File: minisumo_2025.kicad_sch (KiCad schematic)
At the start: 95 parts, among them J1 USB_C Connector, J10 DISTANCE_R90, J11 DISTANCE_R, J12 DISTANCE_RF, J13 DISTANCE_L90, J14 DISTANCE_L, J15 LINE_LEFT, J16 DISTANCE_LF, J2 SERVO, J3 START_MODULE, J4 MOTOR1, J5 MOTOR2, J6 BATT_IN, J8 DISTANCE_CENTER, J9 LINE_RIGHT, SW1 RESET, SW2 CASE, SW5 BOOT, U1 LMR33630ADDAR, U2 USBLC6-2P6, U3 ESP32-S3-WROOM-1, U4 TLV75730PDBVR, U5 TXS0108ERGYR, U6 DRIVER 1, U7 DRIVER 2

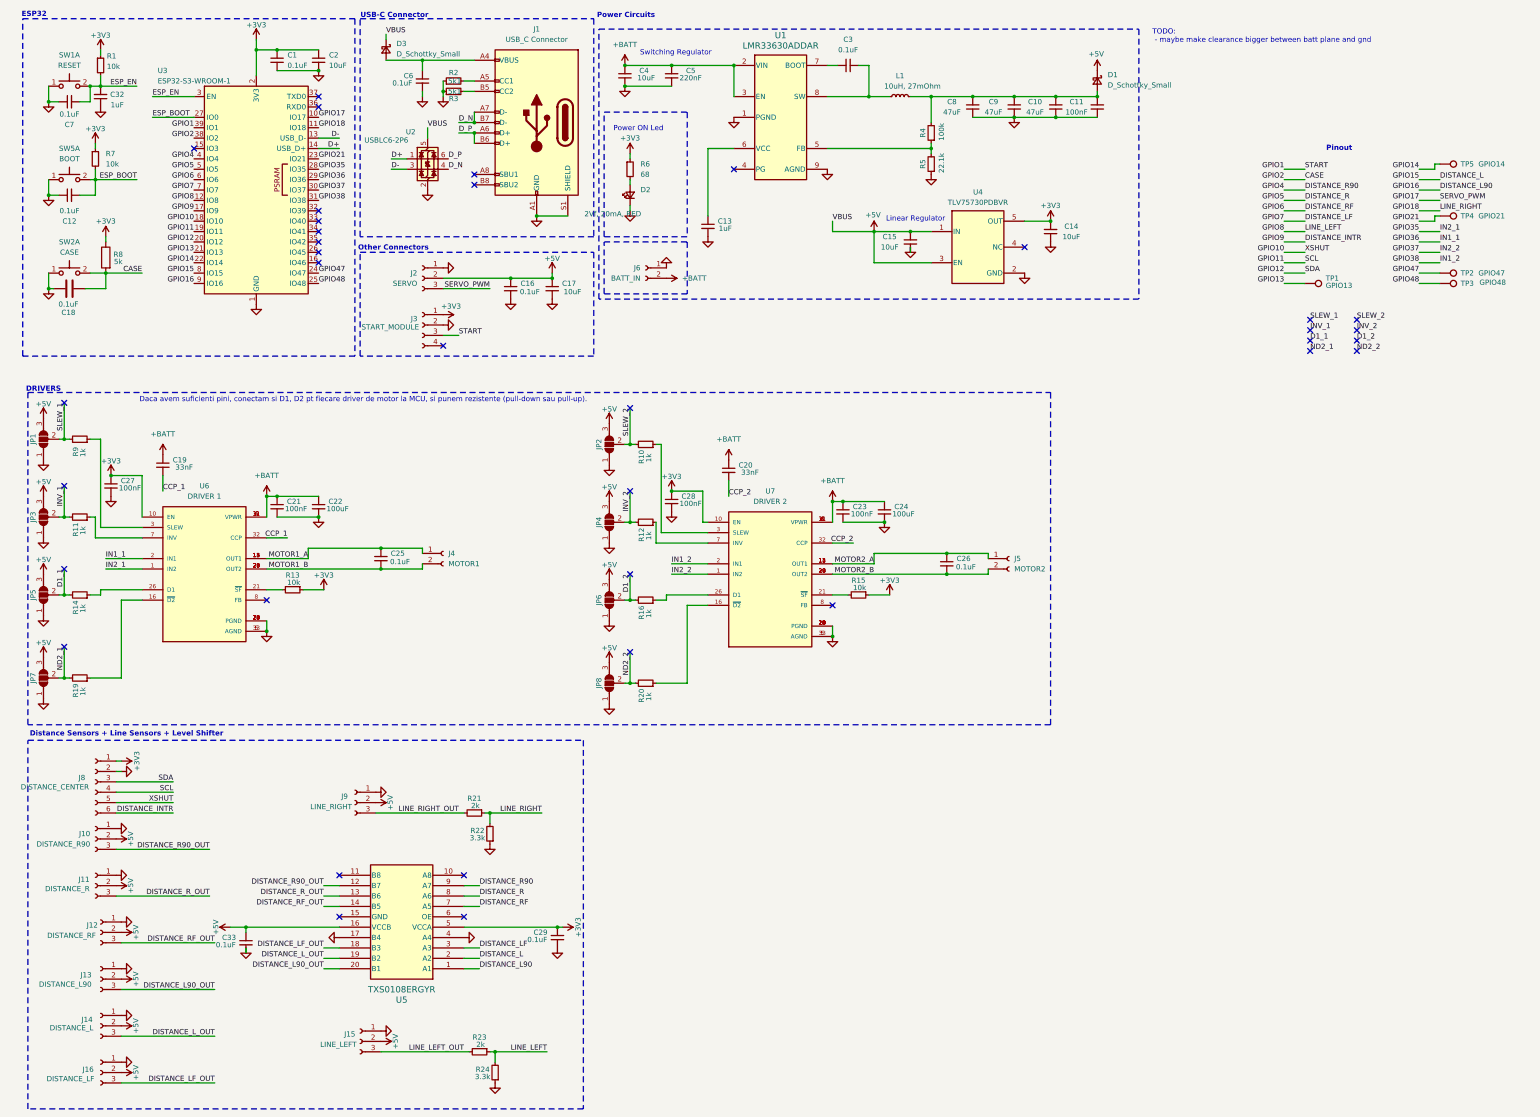
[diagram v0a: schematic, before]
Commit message: added leds for power
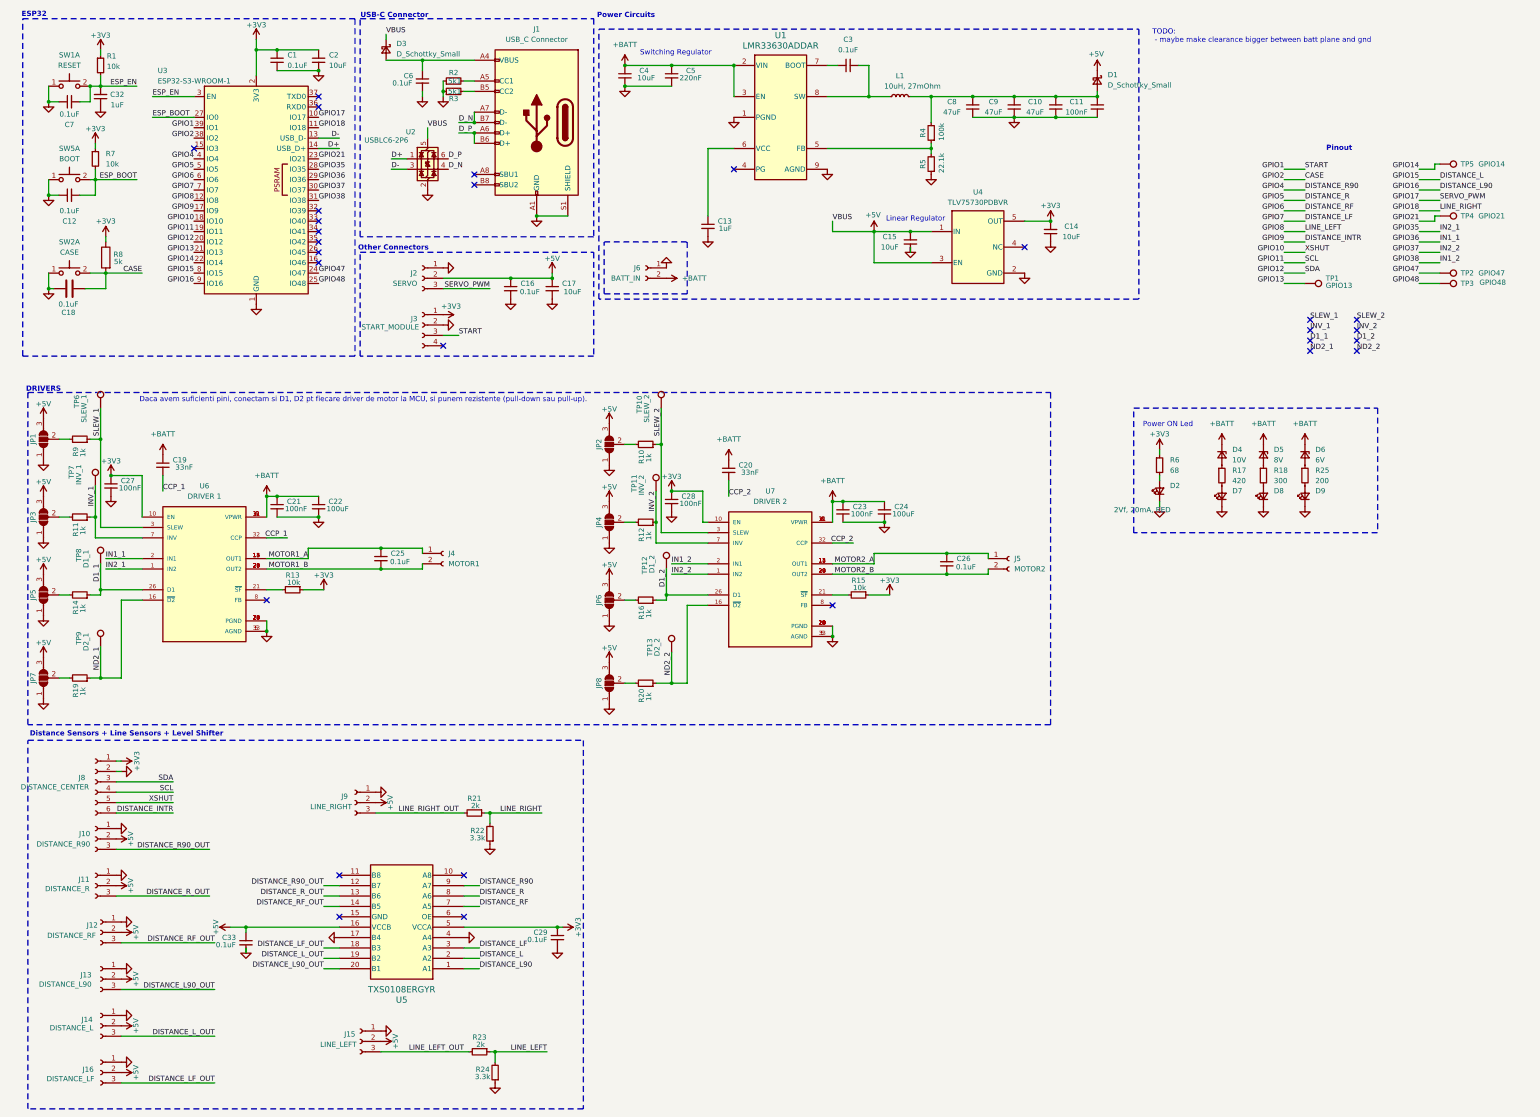
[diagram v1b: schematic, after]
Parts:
- added D4: 10V, Diode_SMD:D_0402_1005Metric, symbol Device:D_Zener_Small
- added D5: 8V, Diode_SMD:D_0402_1005Metric, symbol Device:D_Zener_Small
- added D6: 6V, Diode_SMD:D_0402_1005Metric, symbol Device:D_Zener_Small
- added D7, D8, D9: 2Vf, 20mA, RED, LED_SMD:LED_0603_1608Metric, symbol Device:LED_Small
- added R17: 420, Resistor_SMD:R_0402_1005Metric, symbol Device:R_Small
- added R18: 300, Resistor_SMD:R_0402_1005Metric, symbol Device:R_Small
- added R25: 200, Resistor_SMD:R_0402_1005Metric, symbol Device:R_Small
- added TP10: SLEW_2, TestPoint:TestPoint_Pad_1.5x1.5mm, symbol Connector:TestPoint
- added TP11: INV_2, TestPoint:TestPoint_Pad_1.5x1.5mm, symbol Connector:TestPoint
- added TP12: D1_2, TestPoint:TestPoint_Pad_1.5x1.5mm, symbol Connector:TestPoint
- added TP13: D2_2, TestPoint:TestPoint_Pad_1.5x1.5mm, symbol Connector:TestPoint
- added TP6: SLEW_1, TestPoint:TestPoint_Pad_1.5x1.5mm, symbol Connector:TestPoint
- added TP7: INV_1, TestPoint:TestPoint_Pad_1.5x1.5mm, symbol Connector:TestPoint
- added TP8: D1_1, TestPoint:TestPoint_Pad_1.5x1.5mm, symbol Connector:TestPoint
- added TP9: D2_1, TestPoint:TestPoint_Pad_1.5x1.5mm, symbol Connector:TestPoint
- D2: footprint (none) -> LED_SMD:LED_0603_1608Metric
- R6: footprint (none) -> Resistor_SMD:R_0402_1005Metric
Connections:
- net +BATT: now also D4.1 (K), D5.1 (K), D6.1 (K)
- net D1_1: now also R14.1, U6.26 (D1), TP8.1; no longer JP5.2 (C), R14.2
- net D1_2: now also R16.1, U7.26 (D1), TP12.1; no longer JP6.2 (C), R16.2
- net GND: now also D7.1 (K), D8.1 (K), D9.1 (K)
- net INV_1: now also R11.1, U6.7 (INV), TP7.1; no longer JP3.2 (C), R11.2
- net INV_2: now also R12.1, U7.7 (INV), TP11.1; no longer JP4.2 (C), R12.2
- net ND2_1: now also R19.1, U6.16 (~{D2}), TP9.1; no longer JP7.2 (C), R19.2
- net ND2_2: now also R20.1, U7.16 (~{D2}), TP13.1; no longer JP8.2 (C), R20.2
- net SLEW_1: now also R9.1, U6.3 (SLEW), TP6.1; no longer JP1.2 (C), R9.2
- net SLEW_2: now also R10.1, U7.3 (SLEW), TP10.1; no longer JP2.2 (C), R10.2
- new net: JP7.2 (C), R19.2
- new net: JP2.2 (C), R10.2
- new net: JP3.2 (C), R11.2
- new net: JP4.2 (C), R12.2
- new net: D5.2 (A), R18.1
- new net: D9.2 (A), R25.2
- new net: JP8.2 (C), R20.2
- new net: JP1.2 (C), R9.2
- new net: D8.2 (A), R18.2
- new net: JP5.2 (C), R14.2
- new net: JP6.2 (C), R16.2
- new net: D6.2 (A), R25.1
- new net: D4.2 (A), R17.1
- new net: D7.2 (A), R17.2
- no-connect marks 36 -> 28

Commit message: finished layout
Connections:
- net GND: now also U5.15 (GND), U5.6 (OE); no longer U5.17 (B4), U5.4 (A4)
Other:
- note added: "TODO:"
- note removed: "TODO: - maybe make clearance bigger between batt plane and gnd"

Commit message: silkscreen
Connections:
- net +3V3: now also U5.6 (OE)
- net GND: no longer U5.6 (OE)

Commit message: backup
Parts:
- C1, C12, C16, C18, C25, C26, C29, C3, C33, C6, C7: LCSC Part Number (none) -> C1525
- C10, C8, C9: LCSC Part Number (none) -> C77101
- C11, C21, C23, C27, C28: LCSC Part Number (none) -> C77050
- C13: LCSC Part Number (none) -> C92759
- C14, C15, C17, C4: LCSC Part Number (none) -> C437568
- C19, C20: LCSC Part Number (none) -> C1614
- C2: footprint Capacitor_SMD:C_0402_1005Metric -> Capacitor_SMD:C_0603_1608Metric; LCSC Part Number (none) -> C70225
- C22, C24, J10, J11, J12, J13, J14, J15, J16, J2, J3, J4, J5, J6, J8, J9, JP1, JP2, JP3, JP4, JP5, JP6, JP7, JP8, TP1, TP10, TP11, TP12, TP13, TP2, TP3, TP4, TP5, TP6, TP7, TP8, TP9: now not fitted
- C32: LCSC Part Number (none) -> C14445
- C5: LCSC Part Number (none) -> C1770
- D1, D3: LCSC Part Number (none) -> C389355
- D2, D7, D8, D9: LCSC Part Number (none) -> C2286
- D4: footprint Diode_SMD:D_0402_1005Metric -> Diode_SMD:Nexperia_CFP3_SOD-123W; LCSC Part Number (none) -> C173431
- D5: value 8V -> 8.2V; footprint Diode_SMD:D_0402_1005Metric -> Diode_SMD:Nexperia_CFP3_SOD-123W; LCSC Part Number (none) -> C19077406
- D6: footprint Diode_SMD:D_0402_1005Metric -> Diode_SMD:Nexperia_CFP3_SOD-123W; LCSC Part Number (none) -> C115277
- J1: LCSC Part Number (none) -> C165948
- L1: LCSC Part Number (none) -> C5329540
- R1, R13, R15, R7: LCSC Part Number (none) -> C25531
- R10, R11, R12, R14, R16, R19, R20, R9: LCSC Part Number (none) -> C11702
- R17: value 420 -> 412; LCSC Part Number (none) -> C25112
- R18: LCSC Part Number (none) -> C25102
- R2, R3: footprint Resistor_SMD:R_0603_1608Metric -> Resistor_SMD:R_0402_1005Metric; LCSC Part Number (none) -> C25905
- R21, R23: LCSC Part Number (none) -> C4109
- R22, R24: LCSC Part Number (none) -> C25890
- R25: LCSC Part Number (none) -> C25087
- R4: LCSC Part Number (none) -> C481918
- R5: LCSC Part Number (none) -> C844504
- R6: LCSC Part Number (none) -> C25131
- R8: LCSC Part Number (none) -> C477765
- SW1, SW2, SW5: LCSC Part Number (none) -> C720477
- U1: LCSC Part Number (none) -> C841384
- U2: LCSC Part Number (none) -> C15999
- U3: LCSC Part Number (none) -> C701341
- U4: LCSC Part Number (none) -> C485517
- U5: LCSC Part Number (none) -> C90706
- U6: value DRIVER 1 -> MC33926PNB; LCSC Part Number (none) -> C1556870
- U7: value DRIVER 2 -> MC33926PNB; LCSC Part Number (none) -> C1556870

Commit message: final.
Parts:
- C1, C12, C16, C18, C25, C26, C29, C3, C33, C6, C7: LCSC Part # (none) -> C1525; LCSC Part Number C1525 -> (none)
- C10, C8, C9: LCSC Part # (none) -> C77101; LCSC Part Number C77101 -> (none)
- C11, C21, C23, C27, C28: LCSC Part # (none) -> C77050; LCSC Part Number C77050 -> (none)
- C13: LCSC Part # (none) -> C92759; LCSC Part Number C92759 -> (none)
- C14, C15, C17, C4: LCSC Part # (none) -> C437568; LCSC Part Number C437568 -> (none)
- C19, C20: LCSC Part # (none) -> C1614; LCSC Part Number C1614 -> (none)
- C2: LCSC Part # (none) -> C70225; LCSC Part Number C70225 -> (none)
- C32: LCSC Part # (none) -> C14445; LCSC Part Number C14445 -> (none)
- C5: LCSC Part # (none) -> C1770; LCSC Part Number C1770 -> (none)
- D1, D3: LCSC Part # (none) -> C389355; LCSC Part Number C389355 -> (none)
- D2, D7, D8, D9: LCSC Part # (none) -> C2286; LCSC Part Number C2286 -> (none)
- D4: LCSC Part # (none) -> C173431; LCSC Part Number C173431 -> (none)
- D5: LCSC Part # (none) -> C19077406; LCSC Part Number C19077406 -> (none)
- D6: LCSC Part # (none) -> C115277; LCSC Part Number C115277 -> (none)
- J1: LCSC Part # (none) -> C165948; LCSC Part Number C165948 -> (none)
- L1: LCSC Part # (none) -> C5329540; LCSC Part Number C5329540 -> (none)
- R1, R13, R15, R7: LCSC Part # (none) -> C25531; LCSC Part Number C25531 -> (none)
- R10, R11, R12, R14, R16, R19, R20, R9: LCSC Part # (none) -> C11702; LCSC Part Number C11702 -> (none)
- R17: LCSC Part # (none) -> C25112; LCSC Part Number C25112 -> (none)
- R18: LCSC Part # (none) -> C25102; LCSC Part Number C25102 -> (none)
- R2, R3: LCSC Part # (none) -> C25905; LCSC Part Number C25905 -> (none)
- R21, R23: LCSC Part # (none) -> C4109; LCSC Part Number C4109 -> (none)
- R22, R24: LCSC Part # (none) -> C25890; LCSC Part Number C25890 -> (none)
- R25: LCSC Part # (none) -> C25087; LCSC Part Number C25087 -> (none)
- R4: LCSC Part # (none) -> C481918; LCSC Part Number C481918 -> (none)
- R5: LCSC Part # (none) -> C844504; LCSC Part Number C844504 -> (none)
- R6: LCSC Part # (none) -> C25131; LCSC Part Number C25131 -> (none)
- R8: LCSC Part # (none) -> C477765; LCSC Part Number C477765 -> (none)
- SW1, SW2, SW5: LCSC Part # (none) -> C720477; LCSC Part Number C720477 -> (none)
- U1: LCSC Part # (none) -> C841384; LCSC Part Number C841384 -> (none)
- U2: LCSC Part # (none) -> C15999; LCSC Part Number C15999 -> (none)
- U3: LCSC Part # (none) -> C701341; LCSC Part Number C701341 -> (none)
- U4: LCSC Part # (none) -> C485517; LCSC Part Number C485517 -> (none)
- U5: LCSC Part # (none) -> C90706; LCSC Part Number C90706 -> (none)
- U6, U7: LCSC Part # (none) -> C1556870; LCSC Part Number C1556870 -> (none)

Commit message: saved required changes
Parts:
- removed C33: 0.1uF, Capacitor_SMD:C_0402_1005Metric, symbol Device:C_Small
- removed U5: TXS0108ERGYR, footprints:DQS20_TEX, symbol 2025-02-16_00-59-53:TXB0108DQSR
- added C30: 0.1uF, Capacitor_SMD:C_0402_1005Metric, symbol Device:C_Small
- added U5: TXS0108EPWR, footprints:SOP65P640X120-20N, symbol TXS0108EPWR:TXS0108EPWR
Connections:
- net GPIO35 is gone; now on net GPIO13: U3.28 (IO35), U6.1 (IN2)
- net GPIO36 is gone; now on net GPIO14: U3.29 (IO36), U6.2 (IN1)
- net +3V3: now also U5.10 (OE), U5.2 (VCCA)
- net +5V: now also C30.1, U5.19 (VCCB)
- net DISTANCE_L: now also U3.5 (IO5), U5.3 (A2); no longer U3.8 (IO15)
- net DISTANCE_L90: now also U3.4 (IO4), U5.1 (A1); no longer U3.9 (IO16)
- net DISTANCE_L90_OUT: now also U5.20 (B1)
- net DISTANCE_LF: now also U3.6 (IO6), U5.4 (A3); no longer U3.7 (IO7)
- net DISTANCE_LF_OUT: now also U5.17 (B3)
- net DISTANCE_L_OUT: now also U5.18 (B2)
- net DISTANCE_R: now also U3.8 (IO15), U5.7 (A6); no longer U3.5 (IO5)
- net DISTANCE_R90: now also U3.9 (IO16), U5.8 (A7); no longer U3.4 (IO4)
- net DISTANCE_R90_OUT: now also U5.13 (B7)
- net DISTANCE_RF: now also U3.7 (IO7), U5.6 (A5); no longer U3.6 (IO6)
- net DISTANCE_RF_OUT: now also U5.15 (B5)
- net DISTANCE_R_OUT: now also U5.14 (B6)
- net GND: now also C30.2, U5.11 (GND); no longer J1.S1 (SHIELD), R22.1
- no-connect marks 28 -> 29
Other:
- moved on the sheet: J15, R23, R24

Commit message: more
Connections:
- net GPIO37 is gone; now on net GPIO21: U3.30 (IO37), U7.1 (IN2)
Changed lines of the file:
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@@
 	(wire
 		(pts
-			(xy 355.6 72.39) (xy 360.68 72.39)
+			(xy 355.6 72.39) (xy 374.65 72.39)
 		)
 		(stroke
@@
 		(effects
 			(font
+				(size 1.27 1.27)
+			)
+			(justify left bottom)
+		)
+	)
+	(label "GPIO21"
+		(at 374.65 72.39 0)
+		(effects
+			(font

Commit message: test board layout
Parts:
- removed C16: 0.1uF, Capacitor_SMD:C_0402_1005Metric, symbol Device:C_Small
- removed C17: 10uF, Capacitor_SMD:C_1210_3225Metric, symbol Device:C_Small
- removed J2: SERVO, Connector_JST:JST_XH_B3B-XH-A_1x03_P2.50mm_Vertical, symbol Connector:Conn_01x03_Socket
- removed JP5, JP6, JP7, JP8: SolderJumper_3_Open, Jumper:SolderJumper-3_P1.3mm_Open_RoundedPad1.0x1.5mm_NumberLabels, symbol Jumper:SolderJumper_3_Open
- removed TP2: GPIO47, TestPoint:TestPoint_Pad_1.5x1.5mm, symbol Connector:TestPoint
- removed TP3: GPIO48, TestPoint:TestPoint_Pad_1.5x1.5mm, symbol Connector:TestPoint
- removed TP4: GPIO21, TestPoint:TestPoint_Pad_1.5x1.5mm, symbol Connector:TestPoint
- removed TP5: GPIO14, TestPoint:TestPoint_Pad_1.5x1.5mm, symbol Connector:TestPoint
- added C31: 4.7uF, Capacitor_SMD:C_1210_3225Metric, symbol Device:C_Small
- added C33: 10uF, Capacitor_THT:C_Radial_D6.3mm_H11.0mm_P2.50mm, symbol Device:C_Small
- added D10: 2Vf, 20mA, RED, LED_SMD:LED_0603_1608Metric, symbol Device:LED_Small
- added D11, D12, D13, D14, D15, D16, D17, D18: LED_Small, LED_SMD:LED_0603_1608Metric, symbol Device:LED_Small
- added R26, R27, R28, R29, R30, R31, R32: ?, Resistor_SMD:R_0603_1608Metric, symbol Device:R_Small
- C12, C18, C25, C26, C29, C30, C6, C7: footprint Capacitor_SMD:C_0402_1005Metric -> Capacitor_SMD:C_0603_1608Metric
- C14, C15: footprint Capacitor_SMD:C_1210_3225Metric -> Capacitor_SMD:C_0603_1608Metric
- C22, C24, J10, J11, J12, J13, J14, J15, J16, J3, J4, J5, J6, J8, J9, JP1, JP2, JP3, JP4, TP1, TP10, TP11, TP6, TP7: now fitted
- R1, R10, R11, R12, R13, R15, R17, R18, R2, R21, R22, R23, R24, R25, R3, R4, R5, R6, R7, R8, R9: footprint Resistor_SMD:R_0402_1005Metric -> Resistor_SMD:R_0603_1608Metric
- R14, R16: value 1k -> 10k; footprint Resistor_SMD:R_0402_1005Metric -> Resistor_SMD:R_0603_1608Metric; LCSC Part # C11702 -> C25531
- R19: value 1k -> 68; footprint Resistor_SMD:R_0402_1005Metric -> Resistor_SMD:R_0603_1608Metric; LCSC Part # C11702 -> C25131
- R20: value 1k -> ?; footprint Resistor_SMD:R_0402_1005Metric -> Resistor_SMD:R_0603_1608Metric; LCSC Part # C11702 -> C25131
- TP12: value D1_2 -> GPIO37; now fitted
- TP13: value D2_2 -> GPIO48; now fitted
- TP8: value D1_1 -> GPIO35; now fitted
- TP9: value D2_1 -> GPIO36; now fitted
- U3: footprint RF_Module:ESP32-S3-WROOM-1 -> RF_Module:ESP32-S3-WROOM-1U
- U4: value TLV75730PDBVR -> TLV75733PDBVR
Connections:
- net +3V3: now also U6.16 (~{D2}), U7.16 (~{D2})
- net +BATT: now also C31.2, C33.2
- net DISTANCE_L90_OUT: now also R28.1
- net DISTANCE_LF_OUT: now also R30.1
- net DISTANCE_L_OUT: now also R29.1
- net DISTANCE_R90_OUT: now also R26.1
- net DISTANCE_RF_OUT: now also R27.1
- net DISTANCE_R_OUT: now also R20.1
- net GND: now also R14.1, R16.1, R22.1, U6.26 (D1), U7.26 (D1), C31.1, C33.1, D10.1 (K), D11.1 (K), D12.1 (K), D13.1 (K), D14.1 (K), D15.1 (K), D16.1 (K), D17.1 (K), D18.1 (K)
- net GPIO13: no longer U3.28 (IO35), U6.1 (IN2)
- net GPIO14: now also R19.1; no longer U3.29 (IO36), U6.2 (IN1)
- net GPIO17: now also U6.1 (IN2)
- net GPIO21: now also U6.2 (IN1); no longer U3.30 (IO37), U7.1 (IN2)
- net GPIO47: now also U7.1 (IN2)
- net GPIO48: now also TP13.1
- net LINE_LEFT_OUT: now also R32.1
- net LINE_RIGHT_OUT: now also R31.1
- net at R19.2: now also D10.2 (A)
- net at U7.8 (FB): now also R16.2
- net at R20.2: now also D11.2 (A)
- net at R14.2: now also U6.8 (FB)
- removed net D1_1: R14.1, TP8.1, U6.26 (D1)
- removed net D1_2: R16.1, TP12.1, U7.26 (D1)
- removed net ND2_1: R19.1, TP9.1, U6.16 (~{D2})
- removed net ND2_2: R20.1, TP13.1, U7.16 (~{D2})
- new net: D15.2 (A), R29.2
- new net: D17.2 (A), R31.2
- new net: D16.2 (A), R30.2
- new net: D12.2 (A), R26.2
- new net: D14.2 (A), R28.2
- new net: D13.2 (A), R27.2
- new net: D18.2 (A), R32.2
- new net GPIO35: TP8.1, U3.28 (IO35)
- new net GPIO36: TP9.1, U3.29 (IO36)
- new net GPIO37: TP12.1, U3.30 (IO37)
- no-connect marks 29 -> 19
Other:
- note added: "Sensor indicator leds"
- moved on the sheet: D2, D4, D5, D6, D7, D8, D9, R17, R18, R22, R25, R6
